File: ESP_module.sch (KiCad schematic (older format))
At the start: 13 parts

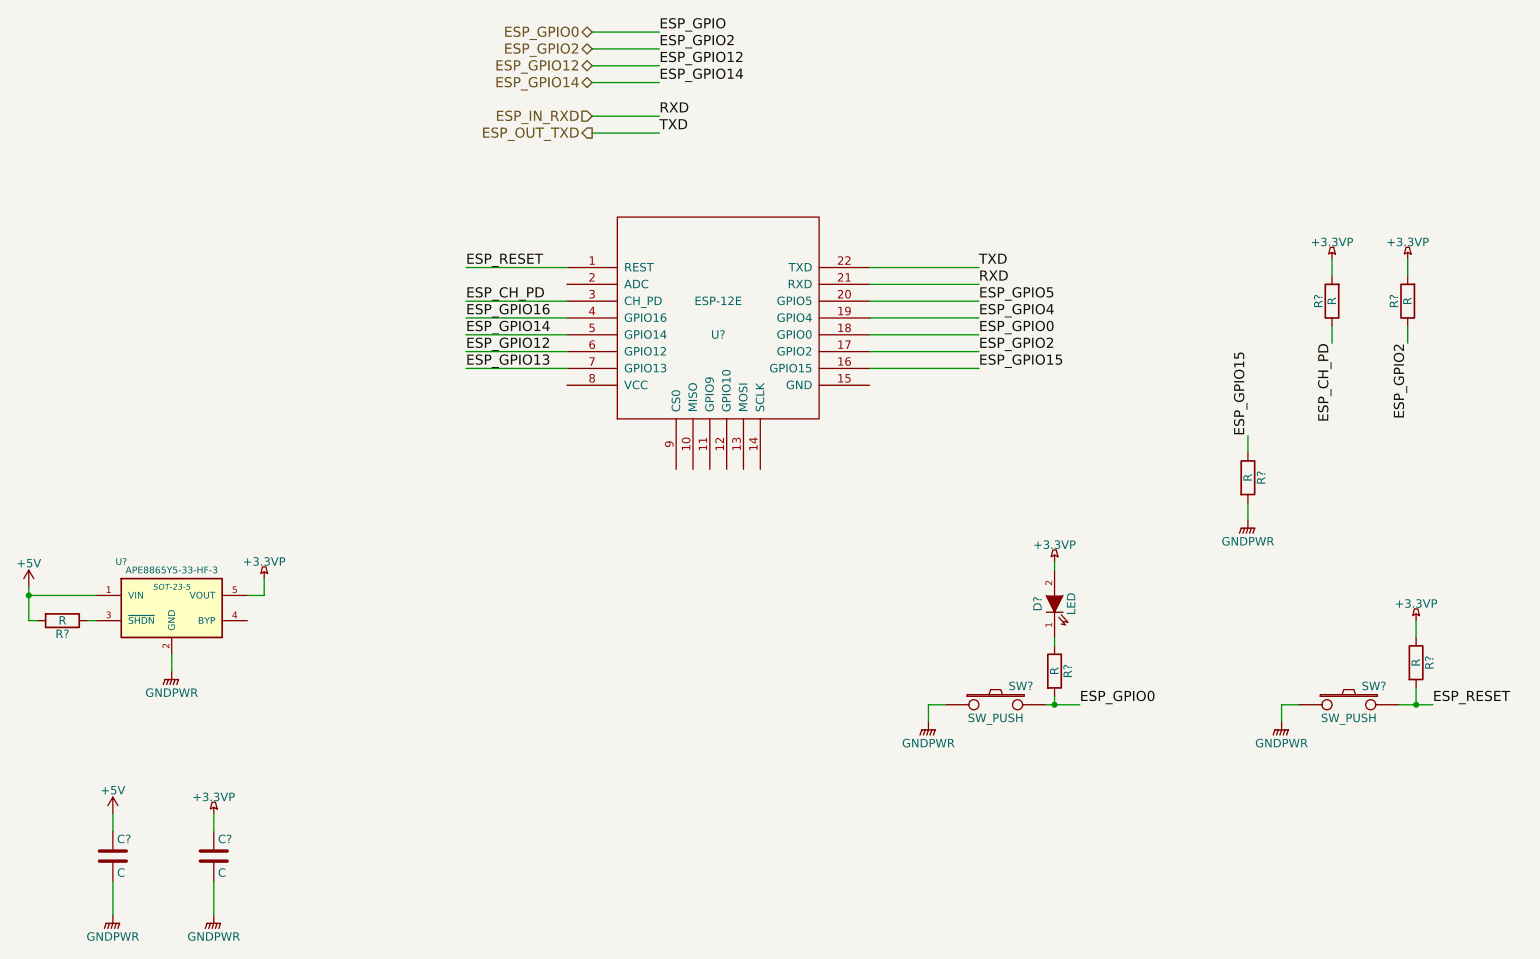
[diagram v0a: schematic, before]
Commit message: Started adding component values and tidying up
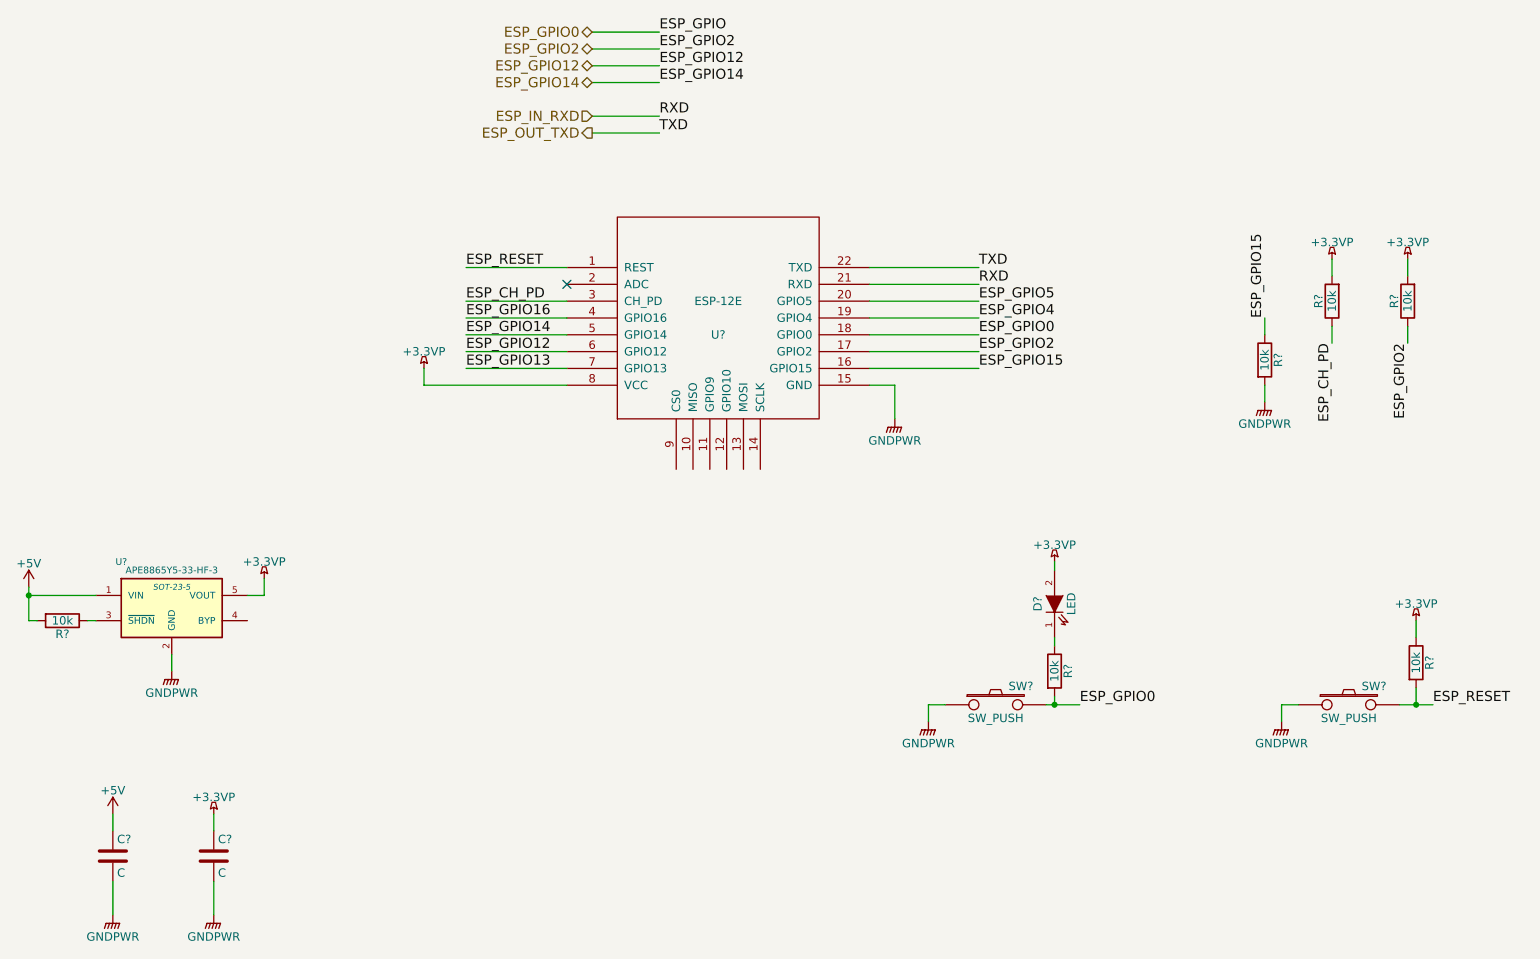
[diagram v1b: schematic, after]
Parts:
- R? (x6): value R -> 10k
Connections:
- net +3.3VP: now also U?.8 (VCC)
- net GNDPWR: now also U?.15 (GND)
- no-connect marks 0 -> 1
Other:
- moved on the sheet: R?
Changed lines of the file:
@@
 P 2150 4450
 F 0 "R?" V 2230 4450 50  0000 C CNN
-F 1 "R" V 2150 4450 50  0000 C CNN
+F 1 "10k" V 2150 4450 50  0000 C CNN
 F 2 "" V 2080 4450 30  0000 C CNN
 F 3 "" H 2150 4450 30  0000 C CNN
@@
 L R R?
 U 1 1 5640085C
-P 9200 3600
-F 0 "R?" V 9280 3600 50  0000 C CNN
-F 1 "R" V 9200 3600 50  0000 C CNN
-F 2 "" V 9130 3600 30  0000 C CNN
-F 3 "" H 9200 3600 30  0000 C CNN
-	1    9200 3600
+P 9300 2900
+F 0 "R?" V 9380 2900 50  0000 C CNN
+F 1 "10k" V 9300 2900 50  0000 C CNN
+F 2 "" V 9230 2900 30  0000 C CNN
+F 3 "" H 9300 2900 30  0000 C CNN
+	1    9300 2900
 	1    0    0    -1
 $EndComp
@@
 L GNDPWR #PWR?
 U 1 1 5640091B
-P 9200 3850
-F 0 "#PWR?" H 9200 3650 50  0001 C CNN
-F 1 "GNDPWR" H 9200 3720 50  0000 C CNN
-F 2 "" H 9200 3800 60  0000 C CNN
-F 3 "" H 9200 3800 60  0000 C CNN
-	1    9200 3850
-	1    0    0    -1
-$EndComp
-Wire Wire Line
-	9200 3750 9200 3850
+P 9300 3150
+F 0 "#PWR?" H 9300 2950 50  0001 C CNN
+F 1 "GNDPWR" H 9300 3020 50  0000 C CNN
+F 2 "" H 9300 3100 60  0000 C CNN
+F 3 "" H 9300 3100 60  0000 C CNN
+	1    9300 3150
+	1    0    0    -1
+$EndComp
+Wire Wire Line
+	9300 3050 9300 3150
 Text Label 7600 2950 0    60   ~ 0
 ESP_GPIO15
 Wire Wire Line
 	6950 2950 7600 2950
-Text Label 9200 3350 1    60   ~ 0
+Text Label 9300 2650 1    60   ~ 0
 ESP_GPIO15
 Wire Wire Line
-	9200 3350 9200 3450
+	9300 2650 9300 2750
 Text Label 4550 2550 0    60   ~ 0
 ESP_CH_PD
@@
 P 9700 2550
 F 0 "R?" V 9780 2550 50  0000 C CNN
-F 1 "R" V 9700 2550 50  0000 C CNN
+F 1 "10k" V 9700 2550 50  0000 C CNN
 F 2 "" V 9630 2550 30  0000 C CNN
 F 3 "" H 9700 2550 30  0000 C CNN
@@
 P 10150 2550
 F 0 "R?" V 10230 2550 50  0000 C CNN
-F 1 "R" V 10150 2550 50  0000 C CNN
+F 1 "10k" V 10150 2550 50  0000 C CNN
 F 2 "" V 10080 2550 30  0000 C CNN
 F 3 "" H 10150 2550 30  0000 C CNN
@@
 P 10200 4700
 F 0 "R?" V 10280 4700 50  0000 C CNN
-F 1 "R" V 10200 4700 50  0000 C CNN
+F 1 "10k" V 10200 4700 50  0000 C CNN
 F 2 "" V 10130 4700 30  0000 C CNN
 F 3 "" H 10200 4700 30  0000 C CNN
@@
 P 8050 4750
 F 0 "R?" V 8130 4750 50  0000 C CNN
-F 1 "R" V 8050 4750 50  0000 C CNN
+F 1 "10k" V 8050 4750 50  0000 C CNN
 F 2 "" V 7980 4750 30  0000 C CNN
 F 3 "" H 8050 4750 30  0000 C CNN
@@
 Wire Wire Line
 	5300 1550 5700 1550
+$Comp
+L +3.3VP #PWR?
+U 1 1 5641AB1C
+P 4300 2950
+F 0 "#PWR?" H 4450 2900 50  0001 C CNN
+F 1 "+3.3VP" H 4300 3050 50  0000 C CNN
+F 2 "" H 4300 2950 60  0000 C CNN
+F 3 "" H 4300 2950 60  0000 C CNN
+	1    4300 2950
+	1    0    0    -1
+$EndComp
+Wire Wire Line
+	4300 2950 4300 3050
+Wire Wire Line
+	4300 3050 5150 3050
+$Comp
+L GNDPWR #PWR?
+U 1 1 5641AB8B
+P 7100 3250
+F 0 "#PWR?" H 7100 3050 50  0001 C CNN
+F 1 "GNDPWR" H 7100 3120 50  0000 C CNN
+F 2 "" H 7100 3200 60  0000 C CNN
+F 3 "" H 7100 3200 60  0000 C CNN
+	1    7100 3250
+	1    0    0    -1
+$EndComp
+Wire Wire Line
+	6950 3050 7100 3050
+Wire Wire Line
+	7100 3050 7100 3250
+NoConn ~ 5150 2450
 $EndSCHEMATC

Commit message: added component values and most packages. Still missing micro usb
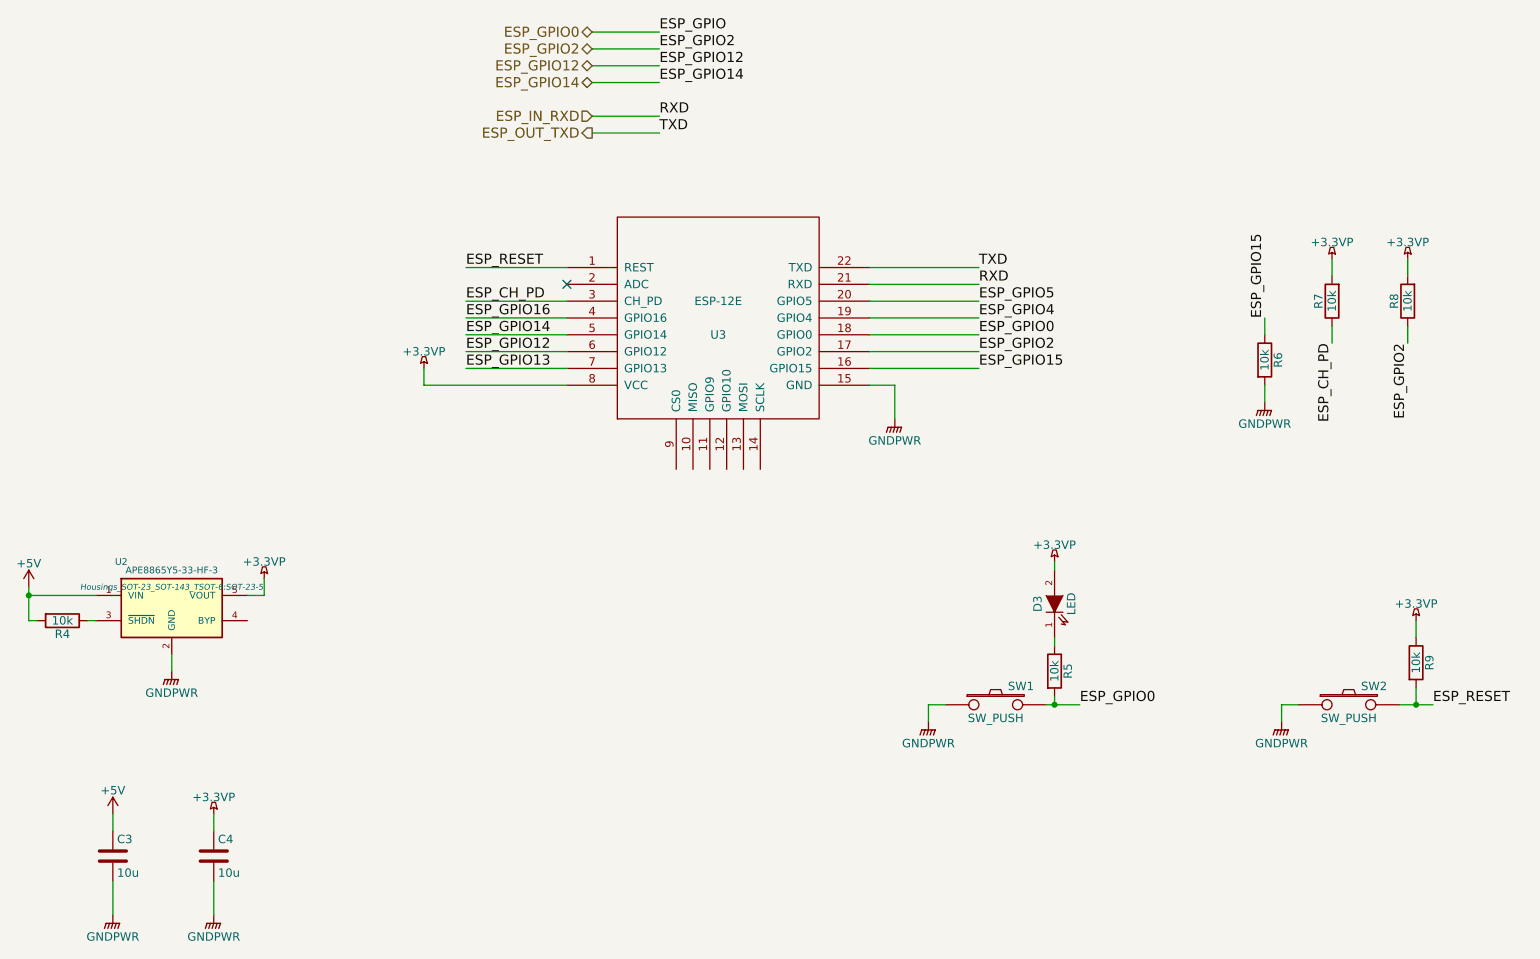
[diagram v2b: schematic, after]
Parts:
- C3, C4: renamed from C?; value C -> 10u; footprint (none) -> Resistors_SMD:R_0603_HandSoldering
- D3: renamed from D?; footprint (none) -> Resistors_SMD:R_0805_HandSoldering
- R4, R5, R6, R7, R8, R9: renamed from R?; footprint (none) -> Resistors_SMD:R_0805_HandSoldering
- SW1, SW2: renamed from SW?; footprint (none) -> Buttons_Switches_SMD:SW_SPST_EVQP2
- U2: renamed from U?; footprint SOT-23-5 -> Housings_SOT-23_SOT-143_TSOT-6:SOT-23-5
- U3: renamed from U?; footprint (none) -> ESP8266:ESP-12E
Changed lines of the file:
@@
 $EndDescr
 $Comp
-L ESP-12E U?
+L ESP-12E U3
 U 1 1 5640040A
 P 6050 2650
-F 0 "U?" H 6050 2550 50  0000 C CNN
+F 0 "U3" H 6050 2550 50  0000 C CNN
 F 1 "ESP-12E" H 6050 2750 50  0000 C CNN
-F 2 "" H 6050 2650 50  0001 C CNN
+F 2 "ESP8266:ESP-12E" H 6050 2650 50  0001 C CNN
 F 3 "" H 6050 2650 50  0001 C CNN
 	1    6050 2650
@@
 $EndComp
 $Comp
-L SW_PUSH SW?
+L SW_PUSH SW2
 U 1 1 5640045D
 P 9800 4950
-F 0 "SW?" H 9950 5060 50  0000 C CNN
+F 0 "SW2" H 9950 5060 50  0000 C CNN
 F 1 "SW_PUSH" H 9800 4870 50  0000 C CNN
-F 2 "" H 9800 4950 60  0000 C CNN
+F 2 "Buttons_Switches_SMD:SW_SPST_EVQP2" H 9800 4950 60  0001 C CNN
 F 3 "" H 9800 4950 60  0000 C CNN
 	1    9800 4950
@@
 $EndComp
 $Comp
-L R R?
+L R R4
 U 1 1 564004F5
 P 2150 4450
-F 0 "R?" V 2230 4450 50  0000 C CNN
+F 0 "R4" V 2230 4450 50  0000 C CNN
 F 1 "10k" V 2150 4450 50  0000 C CNN
-F 2 "" V 2080 4450 30  0000 C CNN
+F 2 "Resistors_SMD:R_0805_HandSoldering" V 2080 4450 30  0001 C CNN
 F 3 "" H 2150 4450 30  0000 C CNN
 	1    2150 4450
@@
 $EndComp
 $Comp
-L C C?
+L C C4
 U 1 1 5640053C
 P 3050 5850
-F 0 "C?" H 3075 5950 50  0000 L CNN
-F 1 "C" H 3075 5750 50  0000 L CNN
-F 2 "" H 3088 5700 30  0000 C CNN
+F 0 "C4" H 3075 5950 50  0000 L CNN
+F 1 "10u" H 3075 5750 50  0000 L CNN
+F 2 "Resistors_SMD:R_0603_HandSoldering" H 3088 5700 30  0001 C CNN
 F 3 "" H 3050 5850 60  0000 C CNN
 	1    3050 5850
@@
 $EndComp
 $Comp
-L APE8865Y5-33-HF-3 U?
+L APE8865Y5-33-HF-3 U2
 U 1 1 5640064F
 P 2800 4350
-F 0 "U?" H 2500 4600 40  0000 C CNN
+F 0 "U2" H 2500 4600 40  0000 C CNN
 F 1 "APE8865Y5-33-HF-3" H 2800 4550 40  0000 C CNN
-F 2 "SOT-23-5" H 2800 4450 35  0000 C CIN
+F 2 "Housings_SOT-23_SOT-143_TSOT-6:SOT-23-5" H 2800 4450 35  0000 C CIN
 F 3 "" H 2800 4350 60  0000 C CNN
 	1    2800 4350
@@
 $EndComp
 $Comp
-L LED D?
+L LED D3
 U 1 1 56400825
 P 8050 4350
-F 0 "D?" H 8050 4450 50  0000 C CNN
+F 0 "D3" H 8050 4450 50  0000 C CNN
 F 1 "LED" H 8050 4250 50  0000 C CNN
-F 2 "" H 8050 4350 60  0000 C CNN
+F 2 "Resistors_SMD:R_0805_HandSoldering" H 8050 4350 60  0001 C CNN
 F 3 "" H 8050 4350 60  0000 C CNN
 	1    8050 4350
@@
 $EndComp
 $Comp
-L R R?
+L R R6
 U 1 1 5640085C
 P 9300 2900
-F 0 "R?" V 9380 2900 50  0000 C CNN
+F 0 "R6" V 9380 2900 50  0000 C CNN
 F 1 "10k" V 9300 2900 50  0000 C CNN
-F 2 "" V 9230 2900 30  0000 C CNN
+F 2 "Resistors_SMD:R_0805_HandSoldering" V 9230 2900 30  0001 C CNN
 F 3 "" H 9300 2900 30  0000 C CNN
 	1    9300 2900
@@
 $EndComp
 $Comp
-L GNDPWR #PWR?
+L GNDPWR #PWR08
 U 1 1 5640091B
 P 9300 3150
-F 0 "#PWR?" H 9300 2950 50  0001 C CNN
+F 0 "#PWR08" H 9300 2950 50  0001 C CNN
 F 1 "GNDPWR" H 9300 3020 50  0000 C CNN
 F 2 "" H 9300 3100 60  0000 C CNN
@@
 	4550 2550 5150 2550
 $Comp
-L R R?
+L R R7
 U 1 1 56400A52
 P 9700 2550
-F 0 "R?" V 9780 2550 50  0000 C CNN
+F 0 "R7" V 9780 2550 50  0000 C CNN
 F 1 "10k" V 9700 2550 50  0000 C CNN
-F 2 "" V 9630 2550 30  0000 C CNN
+F 2 "Resistors_SMD:R_0805_HandSoldering" V 9630 2550 30  0001 C CNN
 F 3 "" H 9700 2550 30  0000 C CNN
 	1    9700 2550
@@
 	9700 2800 9700 2700
 $Comp
-L +3.3VP #PWR?
+L +3.3VP #PWR09
 U 1 1 56400B94
 P 3350 4200
-F 0 "#PWR?" H 3500 4150 50  0001 C CNN
+F 0 "#PWR09" H 3500 4150 50  0001 C CNN
 F 1 "+3.3VP" H 3350 4300 50  0000 C CNN
 F 2 "" H 3350 4200 60  0000 C CNN
@@
 	3350 4300 3250 4300
 $Comp
-L +3.3VP #PWR?
+L +3.3VP #PWR010
 U 1 1 56400CFC
 P 9700 2300
-F 0 "#PWR?" H 9850 2250 50  0001 C CNN
+F 0 "#PWR010" H 9850 2250 50  0001 C CNN
 F 1 "+3.3VP" H 9700 2400 50  0000 C CNN
 F 2 "" H 9700 2300 60  0000 C CNN
@@
 $EndComp
 $Comp
-L R R?
+L R R8
 U 1 1 56400DD6
 P 10150 2550
-F 0 "R?" V 10230 2550 50  0000 C CNN
+F 0 "R8" V 10230 2550 50  0000 C CNN
 F 1 "10k" V 10150 2550 50  0000 C CNN
-F 2 "" V 10080 2550 30  0000 C CNN
+F 2 "Resistors_SMD:R_0805_HandSoldering" V 10080 2550 30  0001 C CNN
 F 3 "" H 10150 2550 30  0000 C CNN
 	1    10150 2550
@@
 	10150 2800 10150 2700
 $Comp
-L +3.3VP #PWR?
+L +3.3VP #PWR011
 U 1 1 56400DDF
 P 10150 2300
-F 0 "#PWR?" H 10300 2250 50  0001 C CNN
+F 0 "#PWR011" H 10300 2250 50  0001 C CNN
 F 1 "+3.3VP" H 10150 2400 50  0000 C CNN
 F 2 "" H 10150 2300 60  0000 C CNN
@@
 	6950 2850 7600 2850
 $Comp
-L R R?
+L R R9
 U 1 1 56400EB2
 P 10200 4700
-F 0 "R?" V 10280 4700 50  0000 C CNN
+F 0 "R9" V 10280 4700 50  0000 C CNN
 F 1 "10k" V 10200 4700 50  0000 C CNN
-F 2 "" V 10130 4700 30  0000 C CNN
+F 2 "Resistors_SMD:R_0805_HandSoldering" V 10130 4700 30  0001 C CNN
 F 3 "" H 10200 4700 30  0000 C CNN
 	1    10200 4700
@@
 $EndComp
 $Comp
-L GNDPWR #PWR?
+L GNDPWR #PWR012
 U 1 1 56400EFA
 P 9400 5050
-F 0 "#PWR?" H 9400 4850 50  0001 C CNN
+F 0 "#PWR012" H 9400 4850 50  0001 C CNN
 F 1 "GNDPWR" H 9400 4920 50  0000 C CNN
 F 2 "" H 9400 5000 60  0000 C CNN
@@
 $EndComp
 $Comp
-L +3.3VP #PWR?
+L +3.3VP #PWR013
 U 1 1 56400F56
 P 10200 4450
-F 0 "#PWR?" H 10350 4400 50  0001 C CNN
+F 0 "#PWR013" H 10350 4400 50  0001 C CNN
 F 1 "+3.3VP" H 10200 4550 50  0000 C CNN
 F 2 "" H 10200 4450 60  0000 C CNN
@@
 Connection ~ 10200 4950
 $Comp
-L SW_PUSH SW?
+L SW_PUSH SW1
 U 1 1 56401146
 P 7700 4950
-F 0 "SW?" H 7850 5060 50  0000 C CNN
+F 0 "SW1" H 7850 5060 50  0000 C CNN
 F 1 "SW_PUSH" H 7700 4870 50  0000 C CNN
-F 2 "" H 7700 4950 60  0000 C CNN
+F 2 "Buttons_Switches_SMD:SW_SPST_EVQP2" H 7700 4950 60  0001 C CNN
 F 3 "" H 7700 4950 60  0000 C CNN
 	1    7700 4950
@@
 $EndComp
 $Comp
-L GNDPWR #PWR?
+L GNDPWR #PWR014
 U 1 1 5640114C
 P 7300 5050
-F 0 "#PWR?" H 7300 4850 50  0001 C CNN
+F 0 "#PWR014" H 7300 4850 50  0001 C CNN
 F 1 "GNDPWR" H 7300 4920 50  0000 C CNN
 F 2 "" H 7300 5000 60  0000 C CNN
@@
 	6950 2750 7600 2750
 $Comp
-L R R?
+L R R5
 U 1 1 56401422
 P 8050 4750
-F 0 "R?" V 8130 4750 50  0000 C CNN
+F 0 "R5" V 8130 4750 50  0000 C CNN
 F 1 "10k" V 8050 4750 50  0000 C CNN
-F 2 "" V 7980 4750 30  0000 C CNN
+F 2 "Resistors_SMD:R_0805_HandSoldering" V 7980 4750 30  0001 C CNN
 F 3 "" H 8050 4750 30  0000 C CNN
 	1    8050 4750
@@
 $EndComp
 $Comp
-L +3.3VP #PWR?
+L +3.3VP #PWR015
 U 1 1 56401476
 P 8050 4100
-F 0 "#PWR?" H 8200 4050 50  0001 C CNN
+F 0 "#PWR015" H 8200 4050 50  0001 C CNN
 F 1 "+3.3VP" H 8050 4200 50  0000 C CNN
 F 2 "" H 8050 4100 60  0000 C CNN
@@
 Connection ~ 8050 4950
 $Comp
-L +3.3VP #PWR?
+L +3.3VP #PWR016
 U 1 1 56401655
 P 3050 5600
-F 0 "#PWR?" H 3200 5550 50  0001 C CNN
+F 0 "#PWR016" H 3200 5550 50  0001 C CNN
 F 1 "+3.3VP" H 3050 5700 50  0000 C CNN
 F 2 "" H 3050 5600 60  0000 C CNN
@@
 $EndComp
 $Comp
-L GNDPWR #PWR?
+L GNDPWR #PWR017
 U 1 1 56401683
 P 3050 6200
-F 0 "#PWR?" H 3050 6000 50  0001 C CNN
+F 0 "#PWR017" H 3050 6000 50  0001 C CNN
 F 1 "GNDPWR" H 3050 6070 50  0000 C CNN
 F 2 "" H 3050 6150 60  0000 C CNN
@@
 $EndComp
 $Comp
-L C C?
+L C C3
 U 1 1 564016F1
 P 2450 5850
-F 0 "C?" H 2475 5950 50  0000 L CNN
-F 1 "C" H 2475 5750 50  0000 L CNN
-F 2 "" H 2488 5700 30  0000 C CNN
+F 0 "C3" H 2475 5950 50  0000 L CNN
+F 1 "10u" H 2475 5750 50  0000 L CNN
+F 2 "Resistors_SMD:R_0603_HandSoldering" H 2488 5700 30  0001 C CNN
 F 3 "" H 2450 5850 60  0000 C CNN
 	1    2450 5850
@@
 $EndComp
 $Comp
-L GNDPWR #PWR?
+L GNDPWR #PWR018
 U 1 1 564016FD
 P 2450 6200
-F 0 "#PWR?" H 2450 6000 50  0001 C CNN
+F 0 "#PWR018" H 2450 6000 50  0001 C CNN
 F 1 "GNDPWR" H 2450 6070 50  0000 C CNN
 F 2 "" H 2450 6150 60  0000 C CNN
@@
 $EndComp
 $Comp
-L +5V #PWR?
+L +5V #PWR019
 U 1 1 564017C3
 P 2450 5600
-F 0 "#PWR?" H 2450 5450 50  0001 C CNN
+F 0 "#PWR019" H 2450 5450 50  0001 C CNN
 F 1 "+5V" H 2450 5740 50  0000 C CNN
 F 2 "" H 2450 5600 60  0000 C CNN
@@
 $EndComp
 $Comp
-L +5V #PWR?
+L +5V #PWR020
 U 1 1 5640181D
 P 1950 4250
-F 0 "#PWR?" H 1950 4100 50  0001 C CNN
+F 0 "#PWR020" H 1950 4100 50  0001 C CNN
 F 1 "+5V" H 1950 4390 50  0000 C CNN
 F 2 "" H 1950 4250 60  0000 C CNN
@@
 	2300 4450 2350 4450
 $Comp
-L GNDPWR #PWR?
+L GNDPWR #PWR021
 U 1 1 564019D4
 P 2800 4750
-F 0 "#PWR?" H 2800 4550 50  0001 C CNN
+F 0 "#PWR021" H 2800 4550 50  0001 C CNN
 F 1 "GNDPWR" H 2800 4620 50  0000 C CNN
 F 2 "" H 2800 4700 60  0000 C CNN
@@
 	5300 1550 5700 1550
 $Comp
-L +3.3VP #PWR?
+L +3.3VP #PWR022
 U 1 1 5641AB1C
 P 4300 2950
-F 0 "#PWR?" H 4450 2900 50  0001 C CNN
+F 0 "#PWR022" H 4450 2900 50  0001 C CNN
 F 1 "+3.3VP" H 4300 3050 50  0000 C CNN
 F 2 "" H 4300 2950 60  0000 C CNN
@@
 	4300 3050 5150 3050
 $Comp
-L GNDPWR #PWR?
+L GNDPWR #PWR023
 U 1 1 5641AB8B
 P 7100 3250
-F 0 "#PWR?" H 7100 3050 50  0001 C CNN
+F 0 "#PWR023" H 7100 3050 50  0001 C CNN
 F 1 "GNDPWR" H 7100 3120 50  0000 C CNN
 F 2 "" H 7100 3200 60  0000 C CNN
